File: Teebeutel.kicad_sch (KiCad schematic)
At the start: 183 parts, among them J1 RJ45_Shielded, J10 RJ45_Shielded, J11 Conn_01x30_Female, J2 USB_A, J3 USB_C_Receptacle_USB2.0, J4 Conn_01x10_Female, J5 Conn_01x10_Female, J6 Conn_01x06_Female, J7 Battery, J8 Conn_01x06_Female, J9 Micro_SD_Card, M1 Motor_DC, Q1 S8050, Q2 S8050, Q3 AO3400, Q4 AO3400, Q5 AO3400, Q6 AO3400, Q7 AO3400, Q8 AO3400, Q9 AO3400, SW1 K1-1506SN-01, SW2 SW_SPST, U1 LIS2DE12, U10 RM-V8xxC_TR1, U11 TLV62569DBVR, U12 SDB628, U13 SGP30, U14 SRV05-4, U2 ESP32-WROOM-32E(16MB), U3 SRV05-4, U4 TXB0104RUT, U5 CH340C, U6 MCP73831-2-OT, U7 PCA9539BS,118, U8 PPSI262, U9 TLV70018_SOT23-5

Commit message: feat(): Update pcb
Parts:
- removed C17: 100nF, Capacitor_SMD:C_0603_1608Metric, symbol Device:C
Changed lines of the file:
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@@
     (pin "2")
-  )
-  (symbol (lib_id "power:VBUS") (at 542.29 34.29 0) (unit 1)
-    (in_bom yes) (on_board yes) (fields_autoplaced)
-    (property "Reference" "#PWR0196" (id 0) (at 542.29 38.1 0)
-      (effects (font (size 1.27 1.27)) hide)
-    )
-    (property "Value" "VBUS" (id 1) (at 542.29 30.6855 0))
-    (property "Footprint" "" (id 2) (at 542.29 34.29 0)
-      (effects (font (size 1.27 1.27)) hide)
-    )
-    (property "Datasheet" "" (id 3) (at 542.29 34.29 0)
-      (effects (font (size 1.27 1.27)) hide)
-    )
-    (pin "1")
   )
   (symbol (lib_name "R_2") (lib_id "Device:R") (at 63.5 39.37 90) (unit 1)
@@
     (pin "1")
   )
-  (symbol (lib_name "C_27") (lib_id "Device:C") (at 542.29 38.1 0) (mirror x) (unit 1)
-    (in_bom yes) (on_board yes)
-    (property "Reference" "C17" (id 0) (at 545.211 39.2684 0)
-      (effects (font (size 1.27 1.27)) (justify left))
-    )
-    (property "Value" "100nF" (id 1) (at 545.211 36.957 0)
-      (effects (font (size 1.27 1.27)) (justify left))
-    )
-    (property "Footprint" "Capacitor_SMD:C_0603_1608Metric" (id 2) (at 543.2552 34.29 0)
-      (effects (font (size 1.27 1.27)) hide)
-    )
-    (property "Datasheet" "~" (id 3) (at 542.29 38.1 0)
-      (effects (font (size 1.27 1.27)) hide)
-    )
-    (property "LCSC" "C14663" (id 5) (at 542.29 38.1 0)
-      (effects (font (size 1.27 1.27)) hide)
-    )
-    (pin "1")
-    (pin "2")
-  )
   (symbol (lib_name "R_36") (lib_id "Device:R") (at 125.73 229.87 0) (mirror y) (unit 1)
     (in_bom yes) (on_board yes) (fields_autoplaced)
@@
     (pin "2")
   )
-  (symbol (lib_name "GND_63") (lib_id "power:GND") (at 542.29 41.91 0) (unit 1)
-    (in_bom yes) (on_board yes)
-    (property "Reference" "#PWR0195" (id 0) (at 542.29 48.26 0)
-      (effects (font (size 1.27 1.27)) hide)
-    )
-    (property "Value" "GND" (id 1) (at 542.417 46.3042 0))
-    (property "Footprint" "" (id 2) (at 542.29 41.91 0)
-      (effects (font (size 1.27 1.27)) hide)
-    )
-    (property "Datasheet" "" (id 3) (at 542.29 41.91 0)
-      (effects (font (size 1.27 1.27)) hide)
-    )
-    (pin "1")
-  )
   (symbol (lib_name "GND_6") (lib_id "power:GND") (at 295.91 26.67 180) (unit 1)
     (in_bom yes) (on_board yes)
@@
       (reference "#PWR0194") (unit 1) (value "VBUS") (footprint "")
     )
-    (path "/f4973c60-5ff3-4445-9c2c-023a1fd65f17"
-      (reference "#PWR0195") (unit 1) (value "GND") (footprint "")
-    )
-    (path "/12d719d6-994a-4520-a970-cebe6b86b3a4"
-      (reference "#PWR0196") (unit 1) (value "VBUS") (footprint "")
-    )
     (path "/3ef7e440-fc48-40b7-8f93-965d9c9f91f9"
       (reference "#PWR0197") (unit 1) (value "GND") (footprint "")
@@
       (reference "C16") (unit 1) (value "100nF") (footprint "Capacitor_SMD:C_0603_1608Metric")
     )
-    (path "/3fe2e164-9407-4432-b6fb-82f17ca78bc9"
-      (reference "C17") (unit 1) (value "100nF") (footprint "Capacitor_SMD:C_0603_1608Metric")
-    )
     (path "/00000000-0000-0000-0000-0000619866a3"

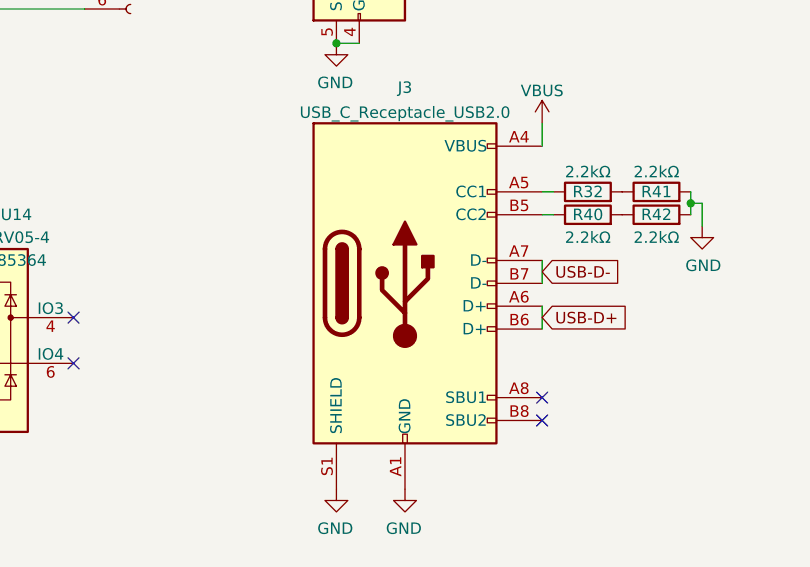
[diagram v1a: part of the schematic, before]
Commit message: chore(): Update / Add partnumbers
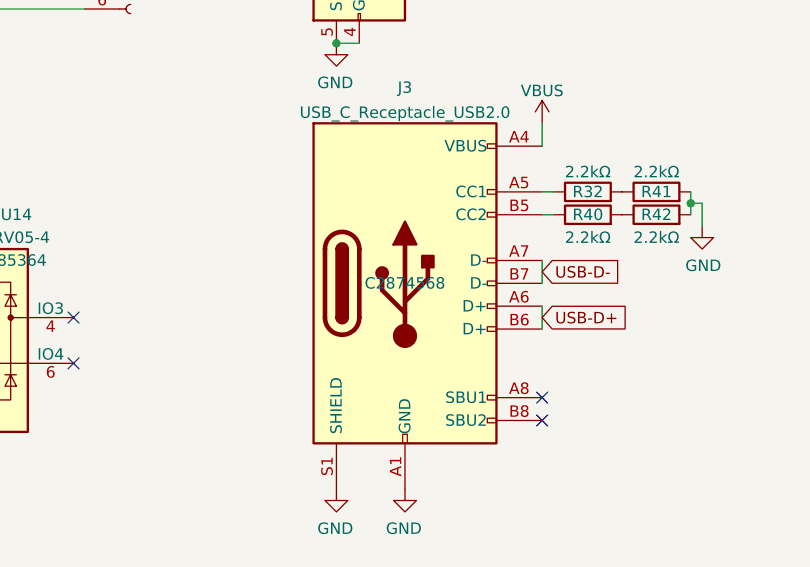
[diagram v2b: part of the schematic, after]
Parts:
- J3: LCSC (none) -> C2874568; Note (none) -> DNP
- J4, J5: MOUSER (none) -> 437-8018301030001101
- J6, J8: MOUSER (none) -> 801-83-006-30-001101
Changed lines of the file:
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@@
+      (effects (font (size 1.27 1.27)) hide)
+    )
+    (property "MOUSER" "437-8018301030001101 " (id 4) (at 274.32 143.51 0)
       (effects (font (size 1.27 1.27)) hide)
     )
@@
       (effects (font (size 1.27 1.27)) hide)
     )
+    (property "MOUSER" "437-8018301030001101" (id 4) (at 271.78 143.51 0)
+      (effects (font (size 1.27 1.27)) hide)
+    )
     (pin "1")
     (pin "10")
@@
       (effects (font (size 1.27 1.27)) hide)
     )
+    (property "MOUSER" " 801-83-006-30-001101 " (id 4) (at 458.47 45.72 0)
+      (effects (font (size 1.27 1.27)) hide)
+    )
     (pin "1")
     (pin "2")
@@
       (effects (font (size 1.27 1.27)) hide)
     )
+    (property "MOUSER" " 801-83-006-30-001101 " (id 4) (at 496.57 45.72 0)
+      (effects (font (size 1.27 1.27)) hide)
+    )
     (pin "1")
     (pin "2")
@@
       (effects (font (size 1.27 1.27)) hide)
     )
+    (property "Note" "DNP" (id 4) (at 527.05 83.82 0)
+      (effects (font (size 1.27 1.27)) hide)
+    )
+    (property "LCSC" "C2874568" (id 5) (at 527.05 83.82 0))
     (pin "A1")
     (pin "A12")

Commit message: feat(): Reassinged refs, cleanup
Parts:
- removed Q1, Q2: S8050, Package_TO_SOT_SMD:SOT-23, symbol Teebeutel_Special_Parts:S8050-J3Y
- added Q3, Q4: AO3400, Package_TO_SOT_SMD:SOT-23, symbol Transistor_FET:BSN20
- J9: renamed from J5; MOUSER 437-8018301030001101 -> 437-8018301030001101
- R15: renamed from R22; value 100kΩ -> 100kΩ 1%
- renumbered C38 to C1, C27 to C10, C31 to C11, C36 to C12, C19 to C13, C44 to C14, C45 to C15, C41 to C16, C39 to C17, C37 to C18, C42 to C19, C4 to C2, C47 to C20, C43 to C21, C1 to C22, C24 to C23, C12 to C24, C21 to C25, C23 to C26, C49 to C27, C22 to C28, C5 to C29, C14 to C3, C33 to C30, C26 to C31, C30 to C32, C29 to C33, C3 to C34, C7 to C35, C10 to C36, C13 to C37, C16 to C38, C20 to C39, C40 to C4, C46 to C40, C32 to C41, C50 to C42, C2 to C43, C6 to C44, C9 to C45, C11 to C46, C15 to C47, C18 to C48, C34 to C49, C8 to C5, C35 to C6, C25 to C7, C28 to C8, C48 to C9, D18 to D13, D19 to D14, D14 to D15, D13 to D16, D20 to D17, D16 to D18, D17 to D19, D15 to D20, F2 to F1, F1 to F2, J10 to J1, J2 to J10, J7 to J11, J1 to J2, J9 to J3, J11 to J4, J3 to J5, J8 to J7, J4 to J8, L2 to L1, L1 to L2, Q3 to Q1, Q4 to Q2, Q6 to Q5, Q7 to Q6, Q5 to Q7, R9 to R1, R23 to R10, R24 to R11, R27 to R12, R28 to R13, R37 to R14, R41 to R16, R32 to R17, R42 to R18, R40 to R19, R1 to R2, R10 to R20, R7 to R21, R33 to R22, R34 to R23, R5 to R24, R21 to R25, R36 to R26, R2 to R27, R3 to R28, R39 to R29, R15 to R3, R12 to R30, R29 to R32, R4 to R33, R6 to R34, R30 to R35, R26 to R36, R25 to R37, R20 to R38, R11 to R39, R16 to R4, R35 to R40, R14 to R41, R38 to R42, R18 to R5, R8 to R6, R13 to R7, R17 to R8, R19 to R9, TP13 to TP10, TP14 to TP11, TP9 to TP12, TP11 to TP13, TP15 to TP14, TP6 to TP15, TP12 to TP16, TP21 to TP17, TP22 to TP18, TP20 to TP19, TP3 to TP2, TP4 to TP20, TP5 to TP21, TP2 to TP22, TP28 to TP23, TP16 to TP24, TP10 to TP25, TP19 to TP26, TP18 to TP27, TP17 to TP28, TP7 to TP3, TP8 to TP4, TP23 to TP5, TP24 to TP6, TP25 to TP7, TP26 to TP8, TP27 to TP9, U14 to U1, U12 to U10, U6 to U12, U10 to U13, U9 to U14, U3 to U2, U4 to U3, U2 to U4, U1 to U6, U13 to U9
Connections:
- net DTR: now also Q4.2 (S)
- net RTS: now also Q3.2 (S)
- net at TP2.1, U4.25 (IO0): now also Q4.3 (D)
- net at TP1.1, U4.3 (EN): now also Q3.3 (D)
- net at R28.1: now also Q4.1 (G)
- net at R27.1: now also Q3.1 (G)

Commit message: chore: Further clean up and BOM reduction
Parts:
- removed C1: 10µF, Capacitor_SMD:C_0603_1608Metric, symbol Device:C
- removed D14, D15: 1N4148WT, Diode_SMD:D_SOD-523, symbol Diode:1N4148WT
- removed D16, D17: DO-214AC, Diode_SMD:D_SMA, symbol Device:D
- removed TP20: I²C SDA, TestPoint:TestPoint_Pad_D1.0mm, symbol Connector:TestPoint
- removed TP21: I²C SCL, TestPoint:TestPoint_Pad_D1.0mm, symbol Connector:TestPoint
- added C15, C16: 10µF, Capacitor_SMD:C_0603_1608Metric, symbol Device:C
- added D17, D18, D19, D20: 1N4148WL, Diode_SMD:D_SOD-123F, symbol Diode:1N4148WT
- C14: renamed from C19; value 22µF -> 10µF; LCSC C59461 -> C19702
- C17: renamed from C20; value 22µF -> 10µF; LCSC C59461 -> C19702
- C18: value 1µF -> 4.7µF; LCSC C15849 -> C19666
- C19: renamed from C17; value 1µF -> 4.7µF; LCSC C15849 -> C19666
- C20: renamed from C14; value 4,7µF -> 4.7µF
- C21: renamed from C15; value 4,7µF -> 4.7µF
- C22: renamed from C16; value 4,7µF -> 4.7µF
- D16: renamed from D13; value 1N4148WT -> 1N4148WL; footprint Diode_SMD:D_SOD-523 -> Diode_SMD:D_SOD-123F; LCSC C727112 -> C108804
- L2: value 4,7µH -> 4.7µH
- R30, R31: value 10Ω -> 56Ω; LCSC C22859 -> C25196
- renumbered C21 to C50, C22 to C51, D18 to D13, D20 to D14, D19 to D15
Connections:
- net +3V3: now also C15.2, D19.1 (K)
- net +5V: now also D17.1 (K)
- net GND: now also C15.1, C16.1, D17.2 (A), D18.1 (K)
- net VPP: now also C16.2, D20.1 (K)
- net at D16.1 (K): now also D18.2 (A)
- net at L2.2, U10.1 (SW): now also D20.2 (A)
- net at M1.2 (-), Q7.3 (D): now also D19.2 (A)
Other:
- moved on the sheet: C24, C3, TP18

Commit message: chore(): Cleanup
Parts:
- J11: LCSC (none) -> C189700
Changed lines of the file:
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@@
   (symbol (lib_id "Connector_Generic:Conn_01x02") (at 326.39 336.55 90) (unit 1)
     (in_bom yes) (on_board yes)
-    (property "Reference" "J11" (id 0) (at 331.1652 337.4644 90)
+    (property "Reference" "J11" (id 0) (at 330.708 336.55 90)
       (effects (font (size 1.27 1.27)) (justify right))
     )
-    (property "Value" "Battery" (id 1) (at 331.1652 339.7758 90)
+    (property "Value" "Battery" (id 1) (at 330.708 338.328 90)
       (effects (font (size 1.27 1.27)) (justify right))
     )
@@
       (effects (font (size 1.27 1.27)) hide)
     )
-    (property "Datasheet" "~" (id 3) (at 326.39 336.55 0)
+    (property "Datasheet" "https://datasheet.lcsc.com/lcsc/1810182031_MOLEX-532610271_C189700.pdf" (id 3) (at 326.39 336.55 0)
       (effects (font (size 1.27 1.27)) hide)
     )
+    (property "LCSC" "C189700" (id 4) (at 335.026 340.36 90))
     (pin "1")
     (pin "2")

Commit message: chore(): Cleanup BOM and update docs
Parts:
- renumbered C2 to C1, C14 to C13, C15 to C14, C16 to C15, C17 to C16, C18 to C17, C20 to C18, C3 to C2, C21 to C20, C22 to C21, C51 to C22, C13 to C3, TP28 to TP20, TP26 to TP21, TP25 to TP23, TP23 to TP25, TP27 to TP26

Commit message: feat(pcb): Lot's of cleanup and rework
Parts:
- added BT1: Battery, symbol Device:Battery
- added J11: Battery, symbol Connector_Generic:Conn_01x02
- J12: renamed from J10; footprint Teebeutel_Special_Parts:on-pcb-USB-A -> Teebeutel_Special_Parts:on-pcb-USB-A-Alignment-Holes
- J2: renamed from J11; footprint Connector_Molex:Molex_PicoBlade_53261-0271_1x02-1MP_P1.25mm_Horizontal -> Connector_JST:JST_PH_S2B-PH-SM4-TB_1x02-1MP_P2.00mm_Horizontal; symbol Connector_Generic:Conn_01x02 -> Connector_Generic_MountingPin:Conn_01x02_MountingPin; LCSC C189700 -> C442222
- J7: renamed from J3; symbol Connector:Micro_SD_Card -> Teebeutel_Special_Parts:Micro_SD_Card_Card_Detect
- TP17: renamed from TP10; value EXP-INT-B -> EXP-INT
- renumbered C8 to C1, C13 to C10, C5 to C11, C1 to C12, C3 to C13, C7 to C14, C2 to C15, C4 to C16, C21 to C17, C19 to C18, C17 to C19, C6 to C2, C18 to C20, C20 to C21, C50 to C22, C22 to C23, C23 to C25, C25 to C26, C26 to C27, C27 to C28, C28 to C29, C12 to C3, C29 to C30, C30 to C31, C31 to C32, C32 to C33, C33 to C34, C34 to C35, C35 to C36, C36 to C37, C37 to C38, C38 to C39, C10 to C4, C39 to C40, C40 to C41, C41 to C42, C42 to C43, C43 to C44, C44 to C45, C45 to C46, C46 to C47, C47 to C48, C48 to C49, C11 to C5, C49 to C50, C15 to C6, C16 to C7, C9 to C8, C14 to C9, D15 to D1, D9 to D13, D3 to D14, D4 to D15, D20 to D16, D19 to D17, D17 to D18, D16 to D19, D14 to D2, D18 to D20, D13 to D3, D6 to D4, D8 to D6, D1 to D7, D2 to D8, D7 to D9, J4 to J1, J8 to J10, J1 to J3, J2 to J4, J6 to J5, J7 to J6, J5 to J8, L2 to L1, L1 to L2, R40 to R1, R39 to R10, R36 to R11, R37 to R12, R32 to R13, R31 to R14, R34 to R15, R33 to R16, R35 to R17, R30 to R18, R24 to R19, R41 to R2, R21 to R20, R20 to R21, R16 to R22, R17 to R23, R18 to R24, R19 to R25, R23 to R26, R22 to R27, R1 to R28, R2 to R29, R42 to R3, R3 to R30, R4 to R31, R5 to R32, R6 to R33, R7 to R34, R8 to R35, R9 to R36, R10 to R37, R11 to R38, R12 to R39, R25 to R4, R13 to R40, R14 to R41, R15 to R42, R26 to R5, R29 to R6, R28 to R7, R27 to R8, R38 to R9, SW2 to SW1, SW1 to SW2, TP18 to TP10, TP12 to TP11, TP13 to TP12, TP14 to TP13, TP16 to TP14, TP17 to TP15, TP19 to TP16, TP11 to TP18, TP21 to TP19, TP22 to TP21, TP15 to TP22, U7 to U1, U12 to U11, U11 to U12, U1 to U13, U2 to U14, U3 to U2, U13 to U3, U8 to U4, U9 to U5, U14 to U6, U5 to U7, U4 to U8, U6 to U9
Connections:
- net GND: now also J2.MP (MountPin), J7.10 (SHIELD); no longer J12.5 (Shield), J7.9 (SHIELD)
- new net: BT1.1 (+), J11.1 (Pin_1)
- new net: BT1.2 (-), J11.2 (Pin_2)
- no-connect marks 27 -> 29

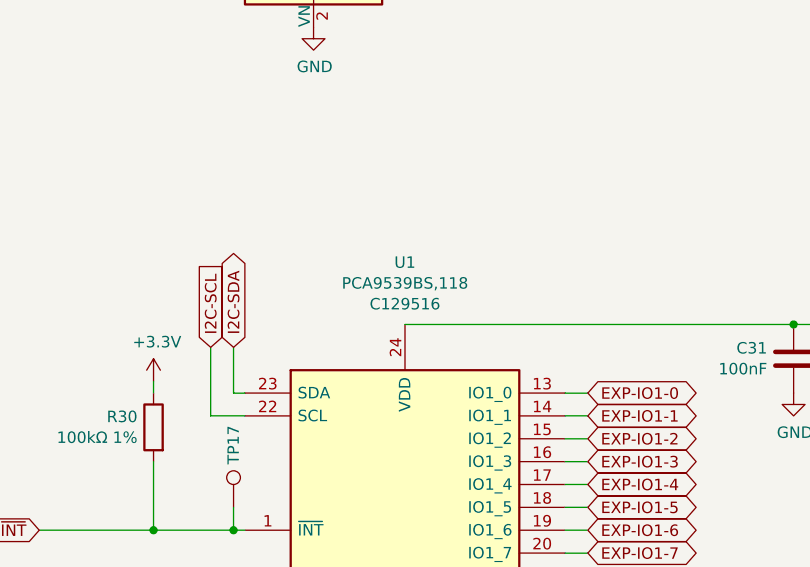
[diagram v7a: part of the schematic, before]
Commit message: chore(sch): Update partnumbers and names
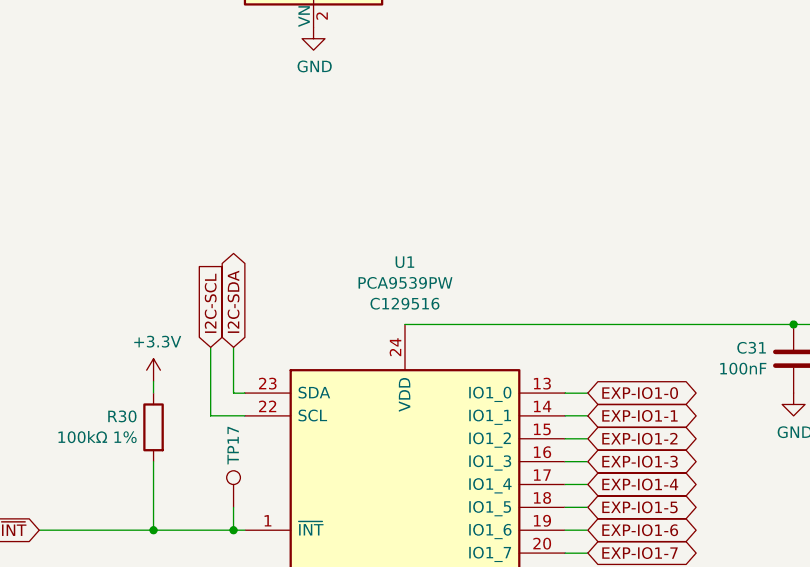
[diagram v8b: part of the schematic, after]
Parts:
- U1: value PCA9539BS,118 -> PCA9539PW
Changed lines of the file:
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@@
     (in_bom yes) (on_board yes)
     (property "Reference" "U1" (id 0) (at 153.67 169.6466 0))
-    (property "Value" "PCA9539BS,118" (id 1) (at 153.67 171.958 0))
+    (property "Value" "PCA9539PW" (id 1) (at 153.67 171.958 0))
     (property "Footprint" "Package_SO:TSSOP-24_4.4x7.8mm_P0.65mm" (id 2) (at 180.34 191.77 0)
       (effects (font (size 1.27 1.27)) (justify left) hide)
@@
     )
     (path "/00000000-0000-0000-0000-000061b3bac9"
-      (reference "U1") (unit 1) (value "PCA9539BS,118") (footprint "Package_SO:TSSOP-24_4.4x7.8mm_P0.65mm")
+      (reference "U1") (unit 1) (value "PCA9539PW") (footprint "Package_SO:TSSOP-24_4.4x7.8mm_P0.65mm")
     )
     (path "/00000000-0000-0000-0000-00006194c291"
